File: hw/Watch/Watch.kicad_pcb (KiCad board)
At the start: 4 copper layers, 192 x 85 mm, 97 parts, among them J1 ESP-Programing_conector, J2 Conn_01x02, J3 Conn_01x04, J7 USB_C_Receptacle_USB2.0, J8 Conn_01x04, Q1 Q_PMOS_DGS-L, Q2 PMOS-2x_BSS84DW, Q3 Q_NMOS_DGS-L, Q5 Q_NMOS_DGS-L, Q6 Q_NMOS_DGS-L, Q7 PMOS-2x_BSS84DW, SW2 EN, SW3 BOOT, SW4 ON, U1 ESP32-S3-MINI, U2 SL8261D-G3JE, U3 LDC1x12, U4 LD39200, U8 BQ25895RTW, U9 TPD4E02B04DQA

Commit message: PCB v0.0.0
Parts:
- moved J8 6.72 mm to (92.8, 45.0)
- moved L2 5.00 mm to (253.1, 50.0)
- moved L1 5.00 mm to (100.0, 50.0)
- moved C3 0.12 mm to (109.5, 90.5)
- moved R7 0.08 mm to (109.5, 89.5)
- renumbered L3 to L1, L1 to L3
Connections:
- net Net-(J8-Pin_1) renamed /L1A
- net Net-(J8-Pin_2) renamed /L1B
- net Net-(J8-Pin_3) renamed /L2A
- net Net-(J8-Pin_4) renamed /L2B
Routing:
- net /L2B: track 171.0 -> 182.5 mm
- net /L2A: track 178.5 -> 189.3 mm
- net /L1B: track 6.70 -> 16.7 mm
- net /L1A: track 14.8 -> 24.1 mm
- net /MainBoard/3V3: track 12.9 -> 17.6 mm, vias 13 -> 16
- net /MainBoard/ESP32-S3-MINI/IO02: track 12.1 -> 10.6 mm
- net /MainBoard/ESP32-S3-MINI/IO10: track 31.5 -> 30.6 mm
- net GND: vias 42 -> 54
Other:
- board size 192 x 85 mm -> 192 x 80 mm

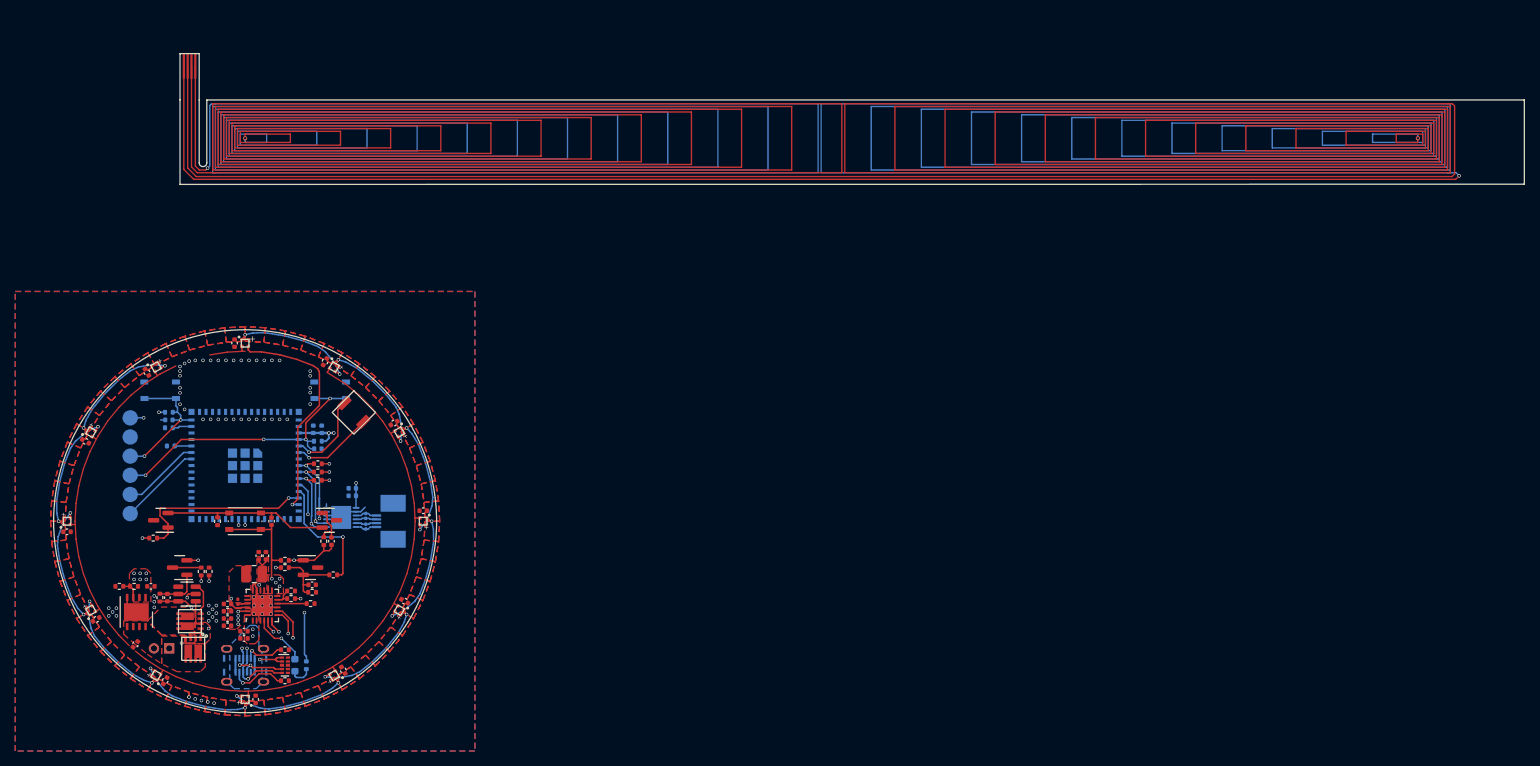
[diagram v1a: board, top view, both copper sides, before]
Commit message: Shift LDO
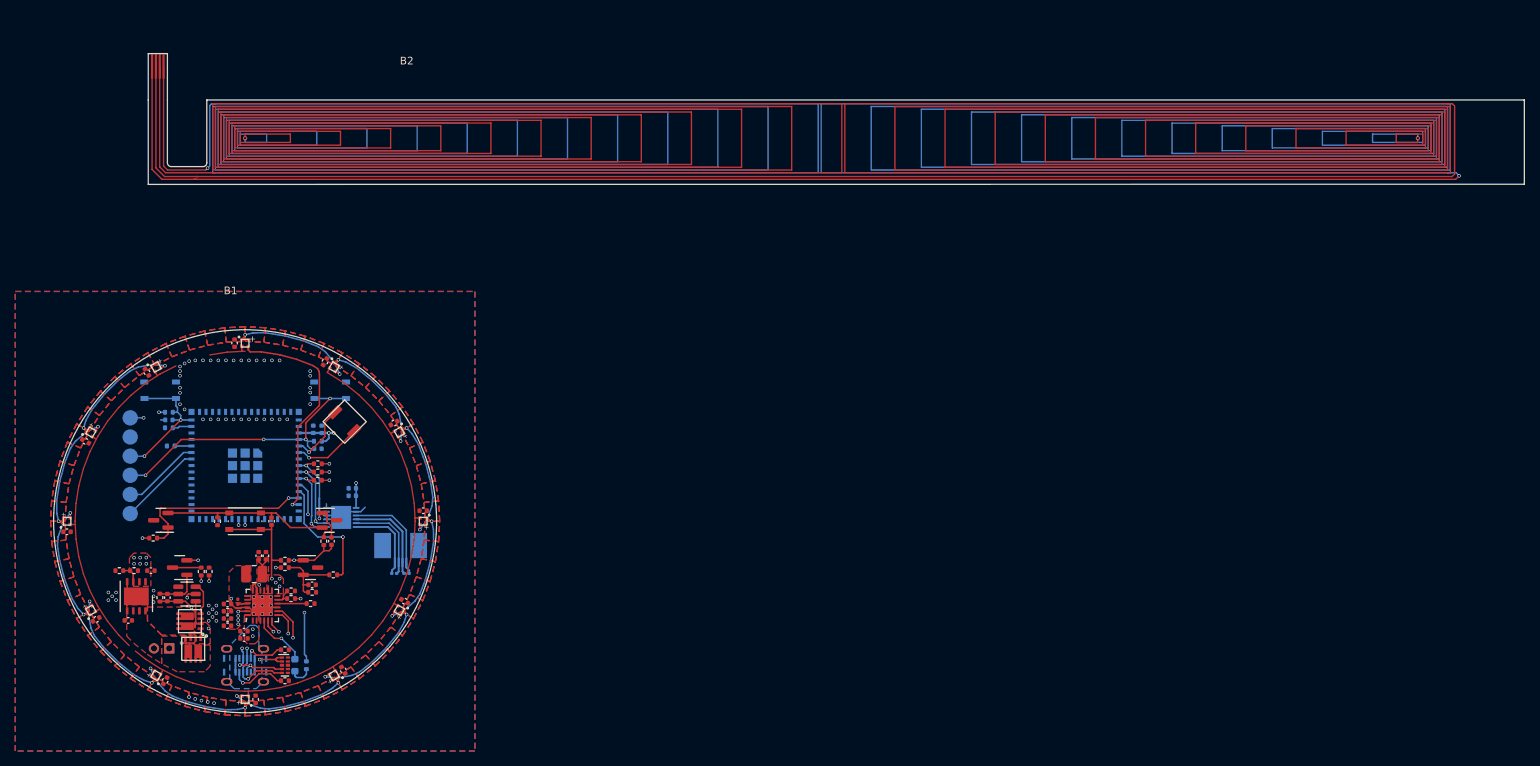
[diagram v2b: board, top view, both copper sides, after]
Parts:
- added B1: ~, RKL-AuxiliarySymbols:Board, F.Cu at (100.0, 75.0)
- added B2: ~, RKL-AuxiliarySymbols:Board, F.Cu at (123.0, 45.0)
- moved C27 9.20 mm to (121.1, 106.8), turned to 0 degrees
- moved C28 7.15 mm to (119.5, 106.8), turned to 0 degrees
- moved J8 4.15 mm to (88.6, 45.0)
- moved C10 3.26 mm to (84.8, 113.0), turned to 180 degrees
- moved C23 2.05 mm to (87.7, 106.5)
- moved R4 2.05 mm to (85.5, 106.5)
- moved R5 2.05 mm to (83.6, 106.5)
- moved U4 2.05 mm to (85.8, 109.8)
- moved J3 1.77 mm to (120.3, 100.5), turned to 0 degrees
- moved BZ1 1.70 mm to (113.0, 87.0)
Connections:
- J3 pad 1: /MainBoard/LC-0A -> /MainBoard/LC-1B
- J3 pad 2: /MainBoard/LC-0B -> /MainBoard/LC-1A
- J3 pad 3: /MainBoard/LC-1A -> /MainBoard/LC-0B
- J3 pad 4: /MainBoard/LC-1B -> /MainBoard/LC-0A
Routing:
- net /MainBoard/LC-0A: track 2.90 -> 13.2 mm
- net /MainBoard/LC-0B: track 2.78 -> 12.3 mm
- net /MainBoard/LC-1A: track 2.78 -> 11.5 mm
- net /MainBoard/LC-1B: track 2.90 -> 10.7 mm
- net /L2B: track 182.5 -> 186.9 mm
- net /L2A: track 189.3 -> 193.6 mm
- net /L1A: track 24.1 -> 28.3 mm
- net /L1B: track 16.7 -> 20.8 mm
- net /MainBoard/ESP32-S3-MINI/IO01: track 11.0 -> 8.33 mm
- net /MainBoard/ESP32-S3-MINI/IO02: track 10.6 -> 8.95 mm
- net GND: track 163.7 -> 162.2 mm
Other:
- outline, holes or cut-outs redrawn

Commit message: WIP
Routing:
- net GND: track 162.2 -> 163.3 mm
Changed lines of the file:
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@@
   (segment (start 106.860177 121.113455) (end 104.615639 121.714877) (width 0.1) (layer "F.Cu") (net 3))
   (segment (start 119.97953 111.044439) (end 119.423532 110.723433) (width 0.2) (layer "F.Cu") (net 3))
-  (segment (start 86.95 117.96) (end 85.66 116.94) (width 0.1) (layer "F.Cu") (net 3))
+  (segment (start 85.145301 116.497815) (end 83.502185 114.854699) (width 0.1) (layer "F.Cu") (net 3))
   (segment (start 101.35 107.99) (end 101.105 108.235) (width 0.2) (layer "F.Cu") (net 3))
   (segment (start 90.970447 120.280709) (end 88.9 119.225764) (width 0.1) (layer "F.Cu") (net 3))
@@
   (segment (start 104.61564 121.714877) (end 102.320532 122.078386) (width 0.1) (layer "F.Cu") (net 3))
   (segment (start 111.044439 80.02047) (end 110.723433 80.576468) (width 0.2) (layer "F.Cu") (net 3))
+  (segment (start 86.951167 117.960177) (end 85.1453 116.497814) (width 0.1) (layer "F.Cu") (net 3))
   (segment (start 101.5 109.0375) (end 101.5 108.657107) (width 0.2) (layer "F.Cu") (net 3))
   (segment (start 102.320532 122.078386) (end 100.43 122.177465) (width 0.1) (layer "F.Cu") (net 3))
   (segment (start 84.6 107.9) (end 84.6 109.05) (width 0.2) (layer "F.Cu") (net 3))
-  (segment (start 84.86 116.23) (end 83.502185 114.8547) (width 0.1) (layer "F.Cu") (net 3))
   (segment (start 80.774236 111.1) (end 79.719291 109.029553) (width 0.1) (layer "F.Cu") (net 3))
   (segment (start 120.280709 109.029553) (end 119.225764 111.1) (width 0.1) (layer "F.Cu") (net 3))
@@
   (segment (start 92.6 109.5) (end 93.55 109.5) (width 0.2) (layer "F.Cu") (net 47))
   (segment (start 92.45 109.65) (end 92.6 109.5) (width 0.2) (layer "F.Cu") (net 47))
+  (segment (start 95.3 107.07) (end 95.3 108.5) (width 0.2) (layer "F.Cu") (net 47))
   (segment (start 92.45 109.975) (end 92.45 109.65) (width 0.2) (layer "F.Cu") (net 47))
-  (segment (start 95.3 107.07) (end 95.3 107.825) (width 0.2) (layer "F.Cu") (net 47))
   (via (at 92.45 109.975) (size 0.45) (drill 0.3) (layers "F.Cu" "B.Cu") (net 47))
-  (via (at 95.3 107.825) (size 0.45) (drill 0.3) (layers "F.Cu" "B.Cu") (net 47))
-  (segment (start 93.15 109.975) (end 92.45 109.975) (width 0.2) (layer "In1.Cu") (net 47))
-  (segment (start 95.3 107.825) (end 93.15 109.975) (width 0.2) (layer "In1.Cu") (net 47))
+  (via (at 95.3 108.5) (size 0.45) (drill 0.3) (layers "F.Cu" "B.Cu") (net 47))
+  (segment (start 95.3 108.5) (end 93.825 109.975) (width 0.2) (layer "In1.Cu") (net 47))
+  (segment (start 93.825 109.975) (end 92.45 109.975) (width 0.2) (layer "In1.Cu") (net 47))
   (segment (start 112.59 107) (end 112.72 106.87) (width 0.2) (layer "F.Cu") (net 48))
   (segment (start 112.72 106.87) (end 112.77 106.82) (width 0.2) (layer "F.Cu") (net 48))

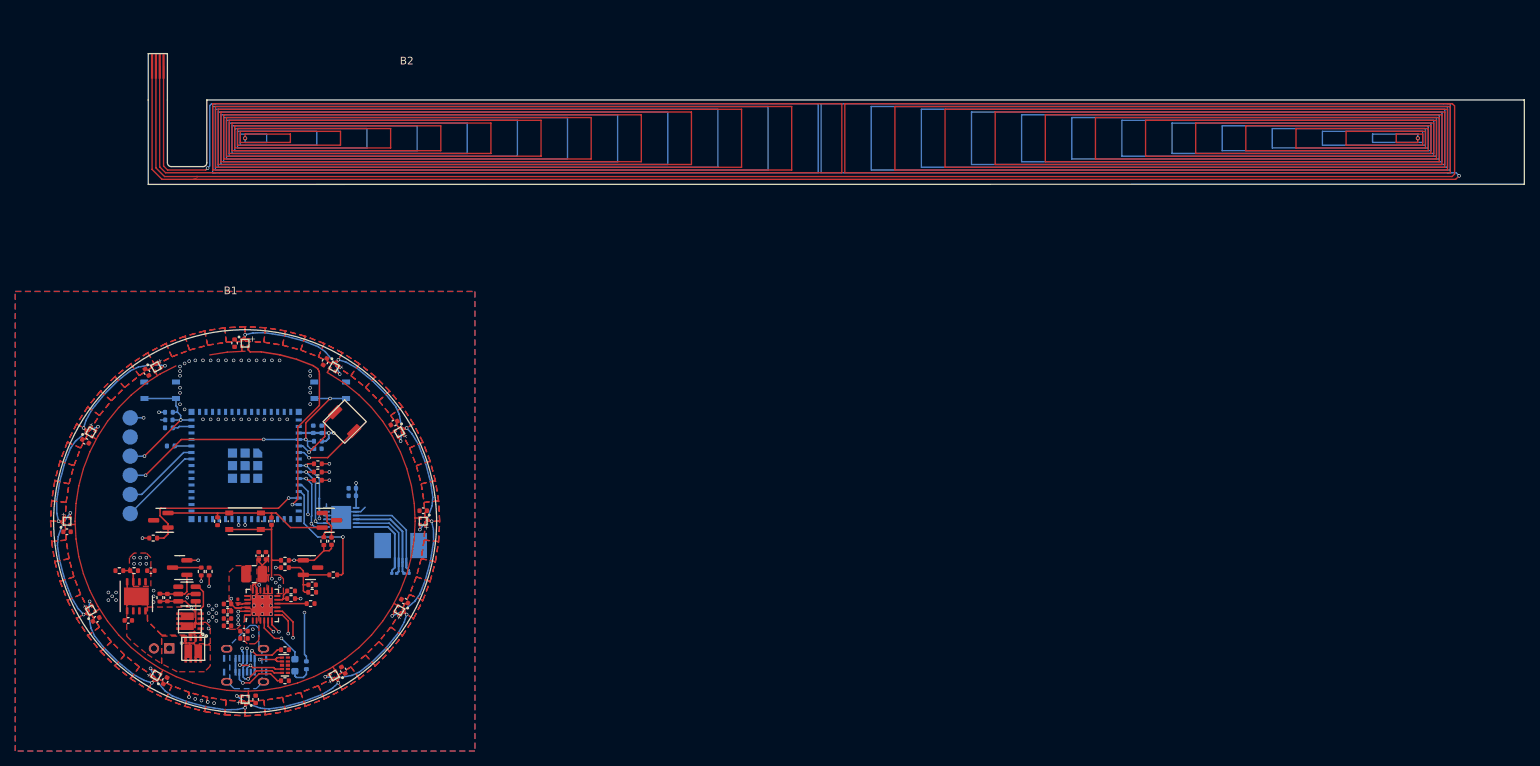
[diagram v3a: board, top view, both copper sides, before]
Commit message: Shift flex connector
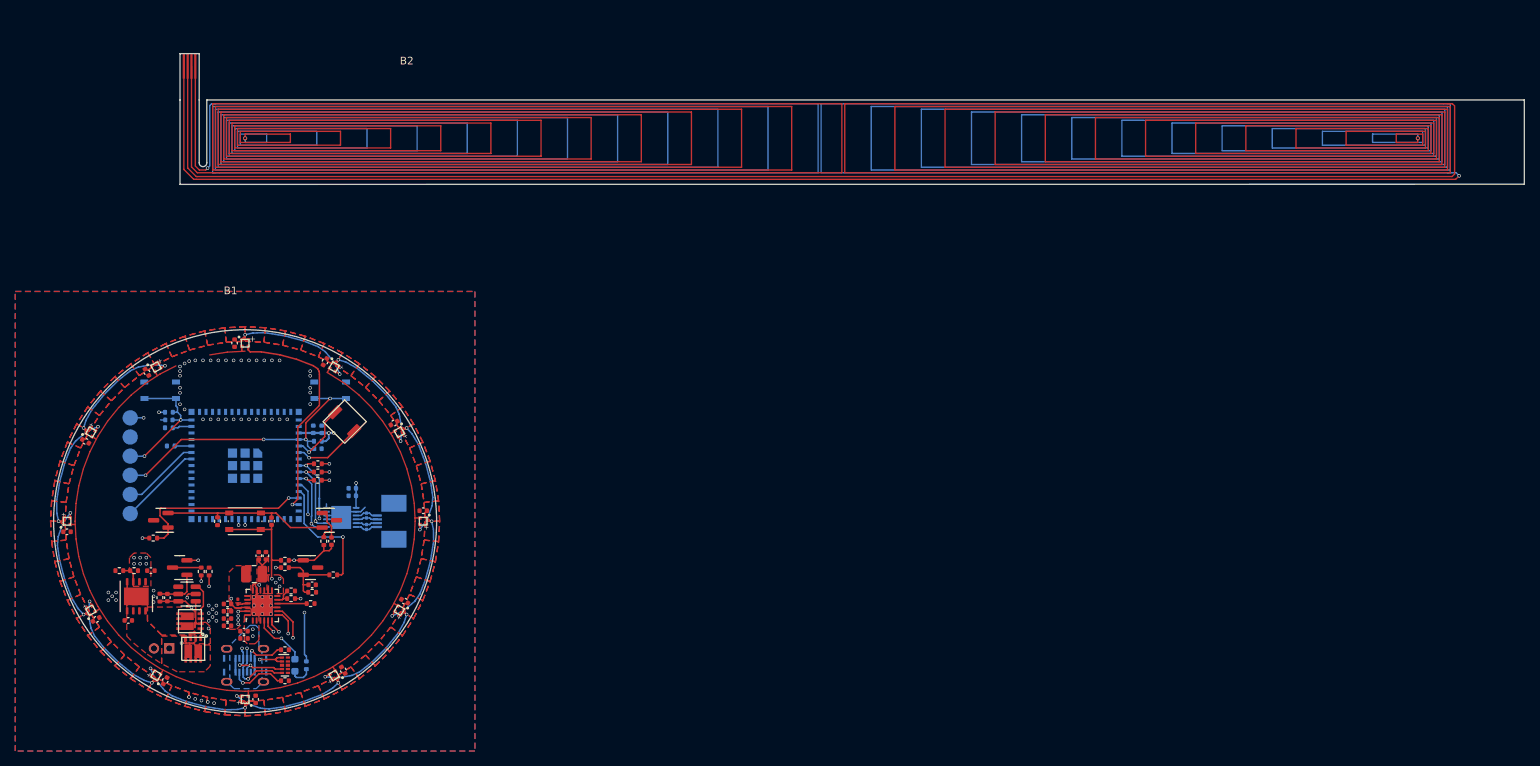
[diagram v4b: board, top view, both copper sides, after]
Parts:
- moved C27 9.18 mm to (115.8, 99.2), turned to 90 degrees
- moved C28 7.05 mm to (115.8, 100.8), turned to 90 degrees
- moved J8 4.15 mm to (92.8, 45.0)
- moved J3 1.86 mm to (122.1, 100.0), turned to -90 degrees
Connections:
- J3 pad 1: /MainBoard/LC-1B -> /MainBoard/LC-0A
- J3 pad 2: /MainBoard/LC-1A -> /MainBoard/LC-0B
- J3 pad 3: /MainBoard/LC-0B -> /MainBoard/LC-1A
- J3 pad 4: /MainBoard/LC-0A -> /MainBoard/LC-1B
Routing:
- net /MainBoard/LC-0A: track 13.2 -> 3.03 mm
- net /MainBoard/LC-0B: track 12.3 -> 2.92 mm
- net /MainBoard/LC-1A: track 11.5 -> 2.92 mm
- net /MainBoard/LC-1B: track 10.7 -> 3.03 mm
- net /L2B: track 186.9 -> 182.5 mm
- net /L2A: track 193.6 -> 189.3 mm
- net /L1A: track 28.3 -> 24.1 mm
- net /L1B: track 20.8 -> 16.7 mm
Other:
- outline, holes or cut-outs redrawn
- board text added: "3V3 GND EN BOOT RX TX"
